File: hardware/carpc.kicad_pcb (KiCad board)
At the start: 2 copper layers, 105.4 x 67.6 mm, 47 parts, among them IC1 ATMEGA328-P, K3 CANBus, P1 PWR_IN, P2 MELBUS, P3 CONN_4, P4 RTI, P5 RELAY_OUT, Q1 BC547, Q2 RELAY, Q3 BC547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

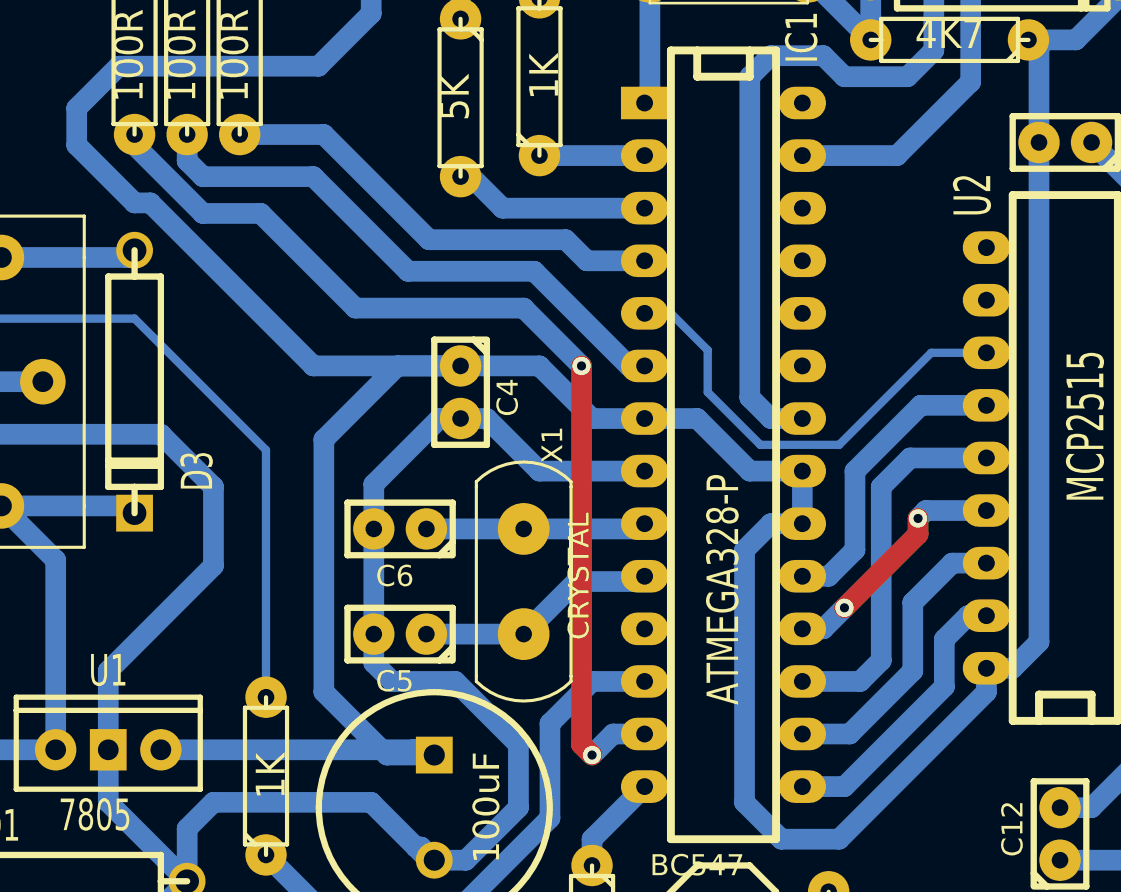
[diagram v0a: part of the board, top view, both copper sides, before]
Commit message: Increased via sizes
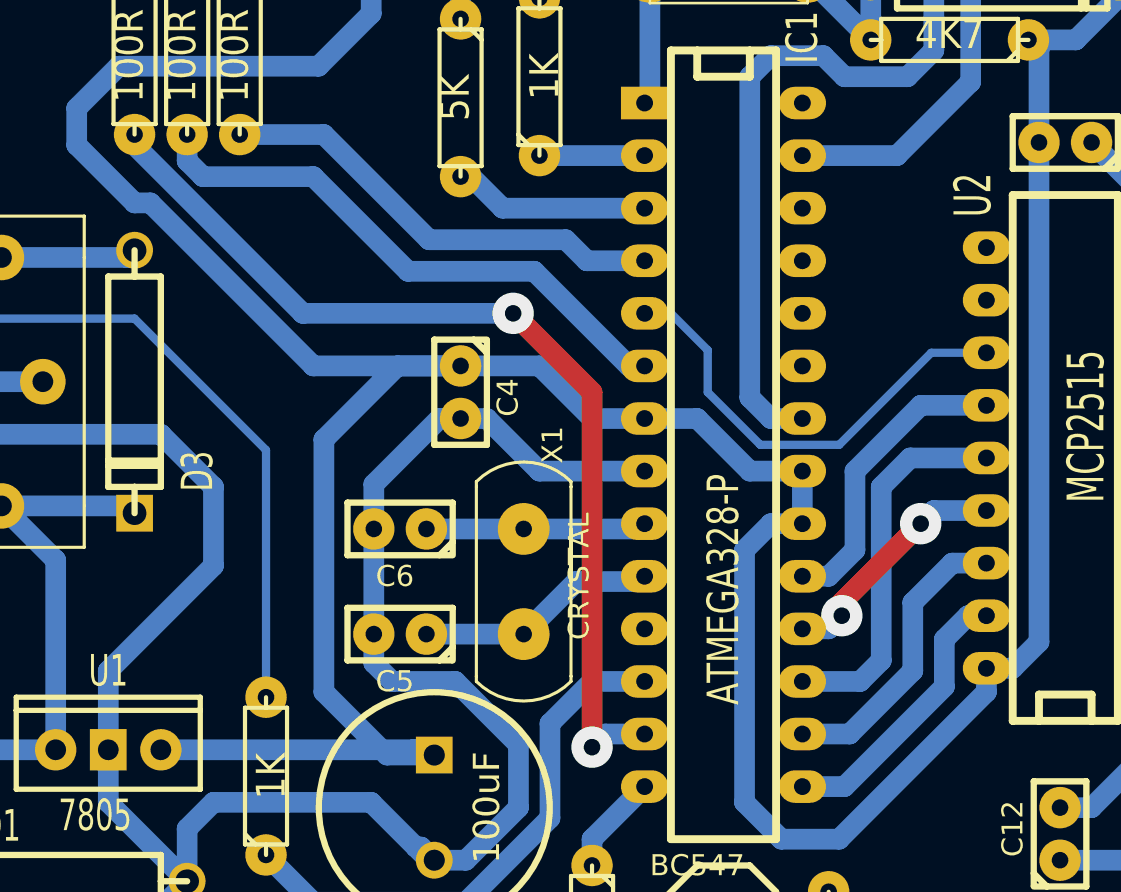
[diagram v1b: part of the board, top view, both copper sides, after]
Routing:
- net /MB_BUSY: track 48.5 -> 47.5 mm
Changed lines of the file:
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@@
     (thickness 1.6)
     (drawings 9)
-    (tracks 311)
+    (tracks 308)
     (zones 0)
     (modules 47)
@@
   )
   (setup
-    (last_trace_width 0.4)
+    (last_trace_width 1)
     (user_trace_width 1)
     (trace_clearance 0.254)
@@
     (via_min_size 0.889)
     (via_min_drill 0.508)
-    (user_via 1.5 0.8)
+    (user_via 2 0.8)
     (uvia_size 0.508)
     (uvia_drill 0.127)
@@
   (segment (start 153.67 90.805) (end 143.51 90.805) (width 1) (layer B.Cu) (net 4))
   (segment (start 154.94 89.535) (end 153.67 90.805) (width 1) (layer B.Cu) (net 4))
-  (segment (start 118.11 92.71) (end 116.586 92.71) (width 1) (layer B.Cu) (net 5))
-  (segment (start 93.472 64.262) (end 93.472 63.754) (width 1) (layer B.Cu) (net 5))
-  (segment (start 96.774 67.564) (end 93.472 64.262) (width 1) (layer B.Cu) (net 5))
-  (segment (start 99.568 67.564) (end 96.774 67.564) (width 1) (layer B.Cu) (net 5))
-  (segment (start 104.14 72.136) (end 99.568 67.564) (width 1) (layer B.Cu) (net 5))
-  (segment (start 112.268 72.136) (end 104.14 72.136) (width 1) (layer B.Cu) (net 5))
-  (segment (start 115.062 74.93) (end 112.268 72.136) (width 1) (layer B.Cu) (net 5))
-  (via (at 115.062 74.93) (size 0.889) (layers F.Cu B.Cu) (net 5))
-  (segment (start 115.062 93.218) (end 115.062 74.93) (width 1) (layer F.Cu) (net 5))
-  (segment (start 115.57 93.726) (end 115.062 93.218) (width 1) (layer F.Cu) (net 5))
-  (via (at 115.57 93.726) (size 0.889) (layers F.Cu B.Cu) (net 5))
-  (segment (start 116.586 92.71) (end 115.57 93.726) (width 1) (layer B.Cu) (net 5))
+  (segment (start 93.472 63.754) (end 93.472 64.262) (width 1) (layer B.Cu) (net 5) (status C00000))
+  (segment (start 116.205 92.71) (end 118.11 92.71) (width 1) (layer B.Cu) (net 5) (status 800000))
+  (segment (start 115.57 93.345) (end 116.205 92.71) (width 1) (layer B.Cu) (net 5))
+  (via (at 115.57 93.345) (size 2) (drill 0.8) (layers F.Cu B.Cu) (net 5))
+  (segment (start 115.57 76.2) (end 115.57 93.345) (width 1) (layer F.Cu) (net 5))
+  (segment (start 111.76 72.39) (end 115.57 76.2) (width 1) (layer F.Cu) (net 5))
+  (via (at 111.76 72.39) (size 2) (drill 0.8) (layers F.Cu B.Cu) (net 5))
+  (segment (start 101.6 72.39) (end 111.76 72.39) (width 1) (layer B.Cu) (net 5))
+  (segment (start 93.472 64.262) (end 101.6 72.39) (width 1) (layer B.Cu) (net 5) (status 400000))
   (segment (start 118.11 69.85) (end 115.316 69.85) (width 1) (layer B.Cu) (net 6))
   (segment (start 102.616 63.754) (end 98.552 63.754) (width 1) (layer B.Cu) (net 6))
@@
   (segment (start 70.612 89.662) (end 74.422 89.662) (width 1) (layer B.Cu) (net 17))
   (segment (start 74.422 89.662) (end 76.962 92.202) (width 1) (layer B.Cu) (net 17))
-  (segment (start 125.73 87.63) (end 126.746 87.63) (width 1) (layer B.Cu) (net 18))
-  (segment (start 131.699 81.915) (end 134.62 81.915) (width 1) (layer B.Cu) (net 18))
-  (segment (start 131.318 82.296) (end 131.699 81.915) (width 1) (layer B.Cu) (net 18))
-  (via (at 131.318 82.296) (size 0.889) (layers F.Cu B.Cu) (net 18))
-  (segment (start 131.318 83.058) (end 131.318 82.296) (width 1) (layer F.Cu) (net 18))
-  (segment (start 127.762 86.614) (end 131.318 83.058) (width 1) (layer F.Cu) (net 18))
-  (via (at 127.762 86.614) (size 0.889) (layers F.Cu B.Cu) (net 18))
-  (segment (start 126.746 87.63) (end 127.762 86.614) (width 1) (layer B.Cu) (net 18))
+  (segment (start 134.62 81.915) (end 132.08 81.915) (width 1) (layer B.Cu) (net 18) (status 400000))
+  (segment (start 127 87.63) (end 125.73 87.63) (width 1) (layer B.Cu) (net 18) (status 800000))
+  (segment (start 127.635 86.995) (end 127 87.63) (width 1) (layer B.Cu) (net 18))
+  (via (at 127.635 86.995) (size 2) (drill 0.8) (layers F.Cu B.Cu) (net 18))
+  (segment (start 127.635 86.36) (end 127.635 86.995) (width 1) (layer F.Cu) (net 18))
+  (segment (start 131.445 82.55) (end 127.635 86.36) (width 1) (layer F.Cu) (net 18))
+  (via (at 131.445 82.55) (size 2) (drill 0.8) (layers F.Cu B.Cu) (net 18))
+  (segment (start 132.08 81.915) (end 131.445 82.55) (width 1) (layer B.Cu) (net 18))
   (segment (start 134.62 79.375) (end 130.937 79.375) (width 1) (layer B.Cu) (net 19))
   (segment (start 128.524 90.17) (end 125.73 90.17) (width 1) (layer B.Cu) (net 19))

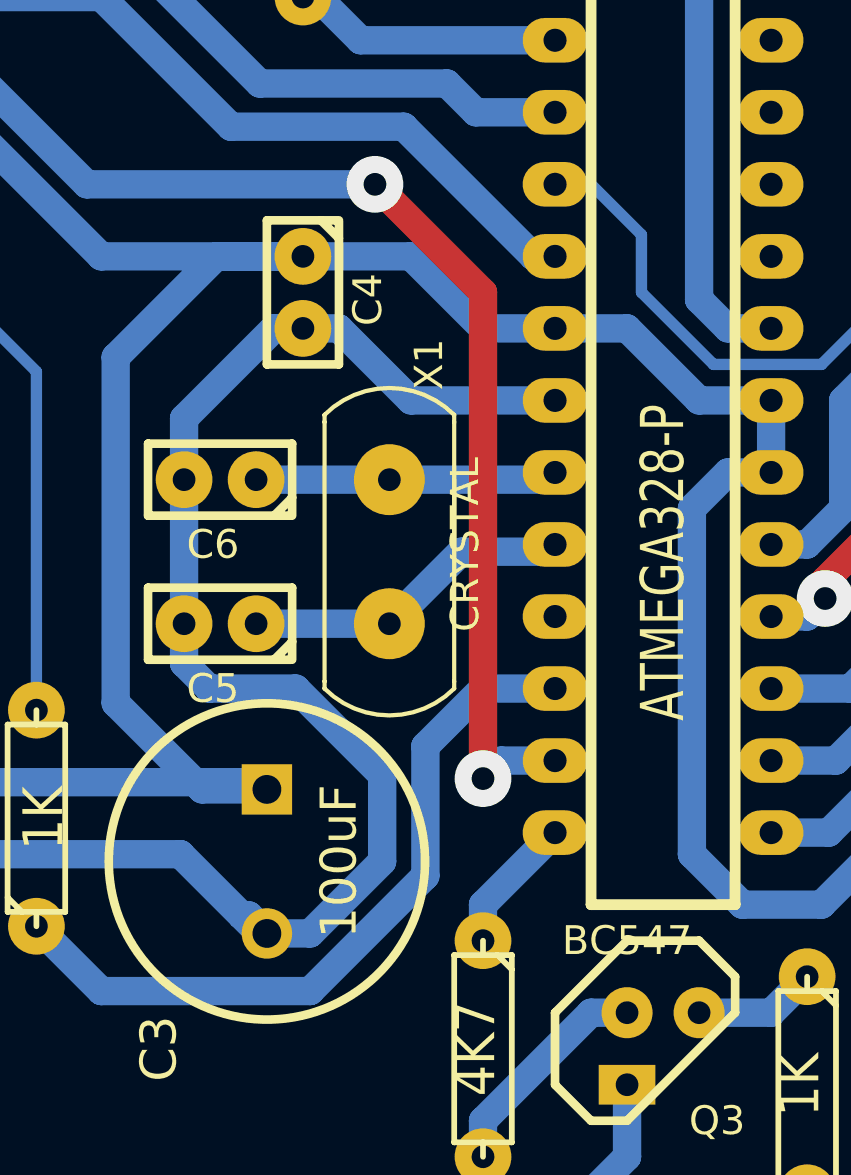
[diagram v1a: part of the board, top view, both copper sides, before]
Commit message: Moved via further from MCU
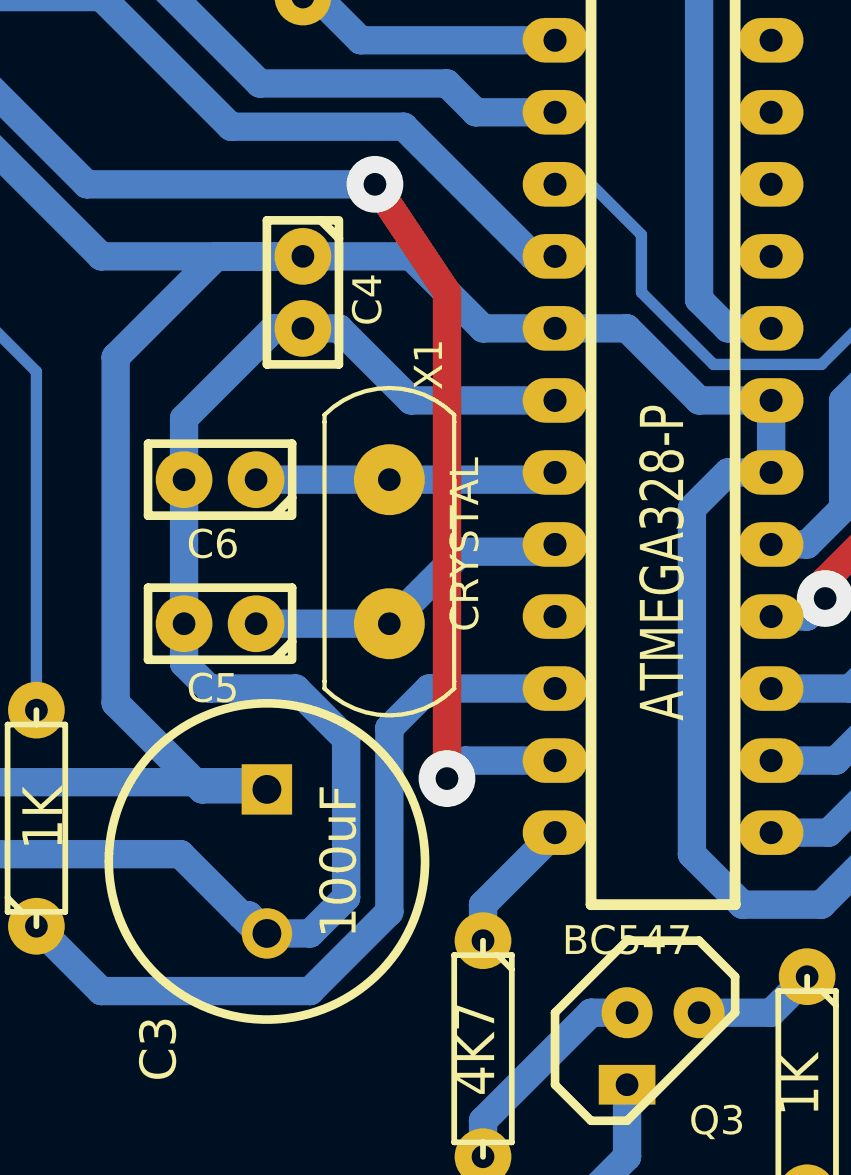
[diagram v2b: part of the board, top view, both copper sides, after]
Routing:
- net /RELAY_OUT: track 26.3 -> 27.4 mm
- net GND: track 356.5 -> 355.5 mm
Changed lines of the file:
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@@
   )
   (setup
-    (last_trace_width 1)
+    (last_trace_width 0.4)
     (user_trace_width 1)
     (trace_clearance 0.254)
@@
   (segment (start 153.67 90.805) (end 143.51 90.805) (width 1) (layer B.Cu) (net 4))
   (segment (start 154.94 89.535) (end 153.67 90.805) (width 1) (layer B.Cu) (net 4))
-  (segment (start 93.472 63.754) (end 93.472 64.262) (width 1) (layer B.Cu) (net 5) (status C00000))
-  (segment (start 116.205 92.71) (end 118.11 92.71) (width 1) (layer B.Cu) (net 5) (status 800000))
-  (segment (start 115.57 93.345) (end 116.205 92.71) (width 1) (layer B.Cu) (net 5))
-  (via (at 115.57 93.345) (size 2) (drill 0.8) (layers F.Cu B.Cu) (net 5))
-  (segment (start 115.57 76.2) (end 115.57 93.345) (width 1) (layer F.Cu) (net 5))
-  (segment (start 111.76 72.39) (end 115.57 76.2) (width 1) (layer F.Cu) (net 5))
+  (segment (start 93.472 63.754) (end 93.472 64.262) (width 1) (layer B.Cu) (net 5))
+  (segment (start 114.935 92.71) (end 118.11 92.71) (width 1) (layer B.Cu) (net 5) (status 800000))
+  (segment (start 114.3 93.345) (end 114.935 92.71) (width 1) (layer B.Cu) (net 5))
+  (via (at 114.3 93.345) (size 2) (drill 0.8) (layers F.Cu B.Cu) (net 5))
+  (segment (start 114.3 76.2) (end 114.3 93.345) (width 1) (layer F.Cu) (net 5))
+  (segment (start 111.76 72.39) (end 114.3 76.2) (width 1) (layer F.Cu) (net 5))
   (via (at 111.76 72.39) (size 2) (drill 0.8) (layers F.Cu B.Cu) (net 5))
   (segment (start 101.6 72.39) (end 111.76 72.39) (width 1) (layer B.Cu) (net 5))
-  (segment (start 93.472 64.262) (end 101.6 72.39) (width 1) (layer B.Cu) (net 5) (status 400000))
+  (segment (start 93.472 64.262) (end 101.6 72.39) (width 1) (layer B.Cu) (net 5))
   (segment (start 118.11 69.85) (end 115.316 69.85) (width 1) (layer B.Cu) (net 6))
   (segment (start 102.616 63.754) (end 98.552 63.754) (width 1) (layer B.Cu) (net 6))
@@
   (segment (start 112.776 70.358) (end 106.68 70.358) (width 1) (layer B.Cu) (net 7))
   (segment (start 117.348 74.93) (end 112.776 70.358) (width 1) (layer B.Cu) (net 7))
-  (segment (start 118.11 90.17) (end 115.57 90.17) (width 1) (layer B.Cu) (net 8))
+  (segment (start 118.11 90.17) (end 113.665 90.17) (width 1) (layer B.Cu) (net 8) (status 400000))
   (segment (start 102.108 100.838) (end 99.822 98.552) (width 1) (layer B.Cu) (net 8))
   (segment (start 109.474 100.838) (end 102.108 100.838) (width 1) (layer B.Cu) (net 8))
-  (segment (start 113.538 96.774) (end 109.474 100.838) (width 1) (layer B.Cu) (net 8))
-  (segment (start 113.538 92.202) (end 113.538 96.774) (width 1) (layer B.Cu) (net 8))
-  (segment (start 115.57 90.17) (end 113.538 92.202) (width 1) (layer B.Cu) (net 8))
+  (segment (start 112.268 98.044) (end 109.474 100.838) (width 1) (layer B.Cu) (net 8))
+  (segment (start 112.268 91.567) (end 112.268 98.044) (width 1) (layer B.Cu) (net 8))
+  (segment (start 113.665 90.17) (end 112.268 91.567) (width 1) (layer B.Cu) (net 8))
   (segment (start 129.032 59.182) (end 129.032 56.388) (width 1) (layer B.Cu) (net 9))
   (segment (start 125.984 56.134) (end 129.032 59.182) (width 1) (layer B.Cu) (net 9))
@@
   (segment (start 105.918 90.17) (end 105.029 89.281) (width 1) (layer B.Cu) (net 17))
   (segment (start 108.966 90.17) (end 105.918 90.17) (width 1) (layer B.Cu) (net 17))
-  (segment (start 112.014 93.218) (end 108.966 90.17) (width 1) (layer B.Cu) (net 17))
-  (segment (start 112.014 96.266) (end 112.014 93.218) (width 1) (layer B.Cu) (net 17))
-  (segment (start 109.474 98.806) (end 112.014 96.266) (width 1) (layer B.Cu) (net 17))
+  (segment (start 110.744 91.948) (end 108.966 90.17) (width 1) (layer B.Cu) (net 17))
+  (segment (start 110.744 97.536) (end 110.744 91.948) (width 1) (layer B.Cu) (net 17))
+  (segment (start 109.474 98.806) (end 110.744 97.536) (width 1) (layer B.Cu) (net 17))
   (segment (start 107.061 98.171) (end 107.315 98.171) (width 1) (layer B.Cu) (net 17))
   (segment (start 107.315 98.171) (end 107.95 98.806) (width 1) (layer B.Cu) (net 17))
@@
   (segment (start 70.612 89.662) (end 74.422 89.662) (width 1) (layer B.Cu) (net 17))
   (segment (start 74.422 89.662) (end 76.962 92.202) (width 1) (layer B.Cu) (net 17))
-  (segment (start 134.62 81.915) (end 132.08 81.915) (width 1) (layer B.Cu) (net 18) (status 400000))
-  (segment (start 127 87.63) (end 125.73 87.63) (width 1) (layer B.Cu) (net 18) (status 800000))
+  (segment (start 134.62 81.915) (end 132.08 81.915) (width 1) (layer B.Cu) (net 18))
+  (segment (start 127 87.63) (end 125.73 87.63) (width 1) (layer B.Cu) (net 18))
   (segment (start 127.635 86.995) (end 127 87.63) (width 1) (layer B.Cu) (net 18))
   (via (at 127.635 86.995) (size 2) (drill 0.8) (layers F.Cu B.Cu) (net 18))
